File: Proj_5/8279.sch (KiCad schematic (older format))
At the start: 24 parts

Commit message: Labeled Data Bus and Address bus wires in CMOS
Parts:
- SW? (x22): symbol Proj_5_Custom_LED:Switch_SW_SPST -> Proj_5-rescue:Switch_SW_SPST-Proj_5_Custom_LED
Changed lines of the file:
@@
 	10050 6550 10050 5500
 $Comp
-L Proj_5_Custom_LED:Switch_SW_SPST SW?
+L Proj_5-rescue:Switch_SW_SPST-Proj_5_Custom_LED SW?
 U 1 1 5EA20375
 P 10250 3000
@@
 $EndComp
 $Comp
-L Proj_5_Custom_LED:Switch_SW_SPST SW?
+L Proj_5-rescue:Switch_SW_SPST-Proj_5_Custom_LED SW?
 U 1 1 5EA1576F
 P 10250 5000
@@
 $EndComp
 $Comp
-L Proj_5_Custom_LED:Switch_SW_SPST SW?
+L Proj_5-rescue:Switch_SW_SPST-Proj_5_Custom_LED SW?
 U 1 1 5EA154A2
 P 10250 4500
@@
 $EndComp
 $Comp
-L Proj_5_Custom_LED:Switch_SW_SPST SW?
+L Proj_5-rescue:Switch_SW_SPST-Proj_5_Custom_LED SW?
 U 1 1 5EA14DD7
 P 10250 4000
@@
 $EndComp
 $Comp
-L Proj_5_Custom_LED:Switch_SW_SPST SW?
+L Proj_5-rescue:Switch_SW_SPST-Proj_5_Custom_LED SW?
 U 1 1 5EA137C2
 P 10250 3500
@@
 	11600 3000 11450 3000
 $Comp
-L Proj_5_Custom_LED:Switch_SW_SPST SW?
+L Proj_5-rescue:Switch_SW_SPST-Proj_5_Custom_LED SW?
 U 1 1 5EA3DD7B
 P 11250 3000
@@
 $EndComp
 $Comp
-L Proj_5_Custom_LED:Switch_SW_SPST SW?
+L Proj_5-rescue:Switch_SW_SPST-Proj_5_Custom_LED SW?
 U 1 1 5EA3DD81
 P 11250 5000
@@
 $EndComp
 $Comp
-L Proj_5_Custom_LED:Switch_SW_SPST SW?
+L Proj_5-rescue:Switch_SW_SPST-Proj_5_Custom_LED SW?
 U 1 1 5EA3DD87
 P 11250 4500
@@
 $EndComp
 $Comp
-L Proj_5_Custom_LED:Switch_SW_SPST SW?
+L Proj_5-rescue:Switch_SW_SPST-Proj_5_Custom_LED SW?
 U 1 1 5EA3DD8D
 P 11250 4000
@@
 $EndComp
 $Comp
-L Proj_5_Custom_LED:Switch_SW_SPST SW?
+L Proj_5-rescue:Switch_SW_SPST-Proj_5_Custom_LED SW?
 U 1 1 5EA3DD93
 P 11250 3500
@@
 	12600 3500 12450 3500
 $Comp
-L Proj_5_Custom_LED:Switch_SW_SPST SW?
+L Proj_5-rescue:Switch_SW_SPST-Proj_5_Custom_LED SW?
 U 1 1 5EA78021
 P 12250 5000
@@
 $EndComp
 $Comp
-L Proj_5_Custom_LED:Switch_SW_SPST SW?
+L Proj_5-rescue:Switch_SW_SPST-Proj_5_Custom_LED SW?
 U 1 1 5EA78027
 P 12250 4500
@@
 $EndComp
 $Comp
-L Proj_5_Custom_LED:Switch_SW_SPST SW?
+L Proj_5-rescue:Switch_SW_SPST-Proj_5_Custom_LED SW?
 U 1 1 5EA7802D
 P 12250 4000
@@
 $EndComp
 $Comp
-L Proj_5_Custom_LED:Switch_SW_SPST SW?
+L Proj_5-rescue:Switch_SW_SPST-Proj_5_Custom_LED SW?
 U 1 1 5EA78033
 P 12250 3500
@@
 	13600 3500 13450 3500
 $Comp
-L Proj_5_Custom_LED:Switch_SW_SPST SW?
+L Proj_5-rescue:Switch_SW_SPST-Proj_5_Custom_LED SW?
 U 1 1 5EA82E83
 P 13250 5000
@@
 $EndComp
 $Comp
-L Proj_5_Custom_LED:Switch_SW_SPST SW?
+L Proj_5-rescue:Switch_SW_SPST-Proj_5_Custom_LED SW?
 U 1 1 5EA82E89
 P 13250 4500
@@
 $EndComp
 $Comp
-L Proj_5_Custom_LED:Switch_SW_SPST SW?
+L Proj_5-rescue:Switch_SW_SPST-Proj_5_Custom_LED SW?
 U 1 1 5EA82E8F
 P 13250 4000
@@
 $EndComp
 $Comp
-L Proj_5_Custom_LED:Switch_SW_SPST SW?
+L Proj_5-rescue:Switch_SW_SPST-Proj_5_Custom_LED SW?
 U 1 1 5EA82E95
 P 13250 3500
@@
 	14650 3500 14500 3500
 $Comp
-L Proj_5_Custom_LED:Switch_SW_SPST SW?
+L Proj_5-rescue:Switch_SW_SPST-Proj_5_Custom_LED SW?
 U 1 1 5EA89F25
 P 14300 5000
@@
 $EndComp
 $Comp
-L Proj_5_Custom_LED:Switch_SW_SPST SW?
+L Proj_5-rescue:Switch_SW_SPST-Proj_5_Custom_LED SW?
 U 1 1 5EA89F2B
 P 14300 4500
@@
 $EndComp
 $Comp
-L Proj_5_Custom_LED:Switch_SW_SPST SW?
+L Proj_5-rescue:Switch_SW_SPST-Proj_5_Custom_LED SW?
 U 1 1 5EA89F31
 P 14300 4000
@@
 $EndComp
 $Comp
-L Proj_5_Custom_LED:Switch_SW_SPST SW?
+L Proj_5-rescue:Switch_SW_SPST-Proj_5_Custom_LED SW?
 U 1 1 5EA89F37
 P 14300 3500

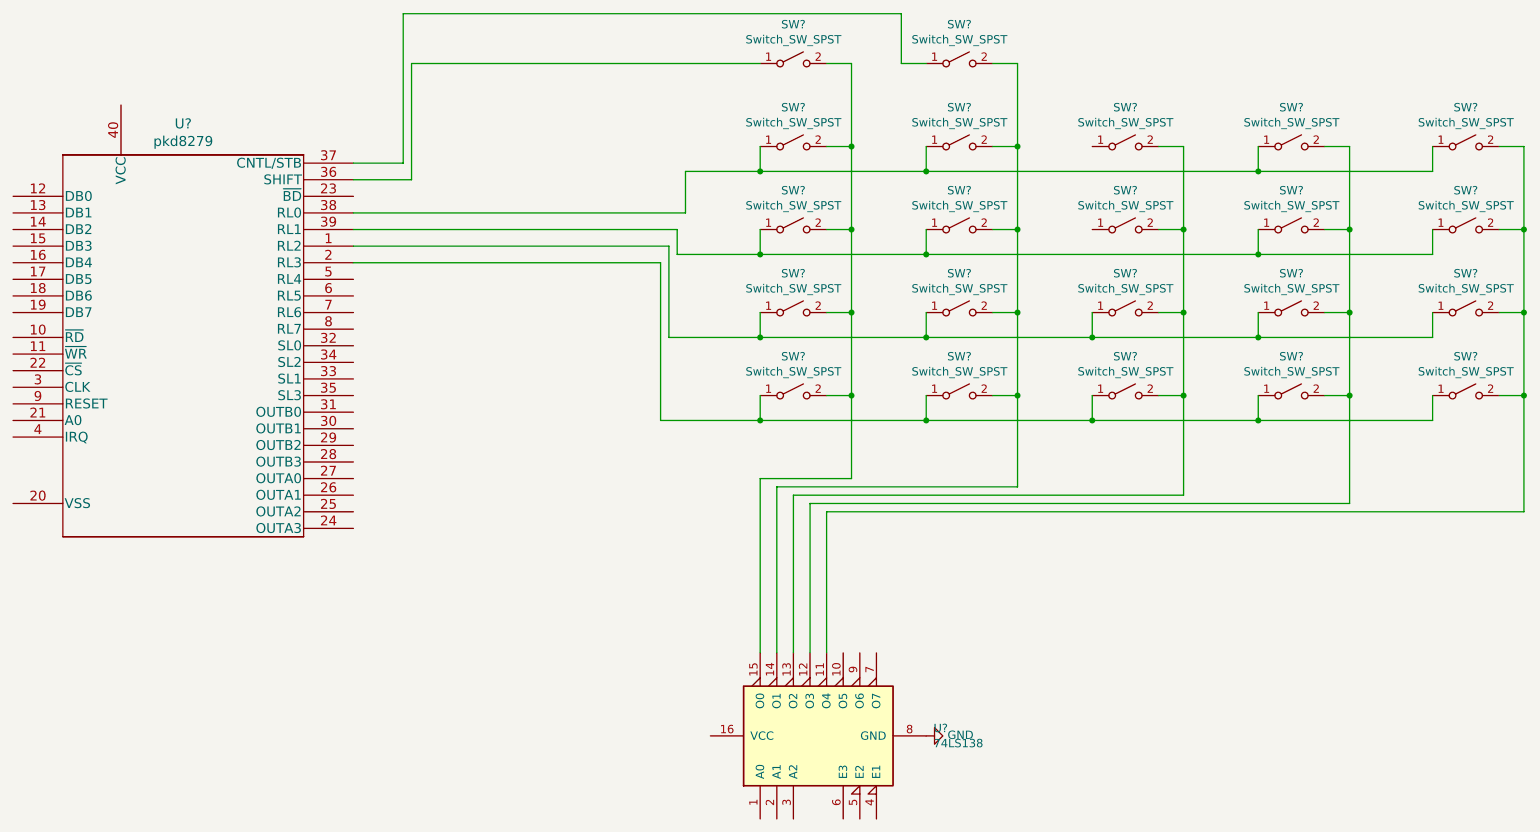
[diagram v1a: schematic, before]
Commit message: Added address decoding
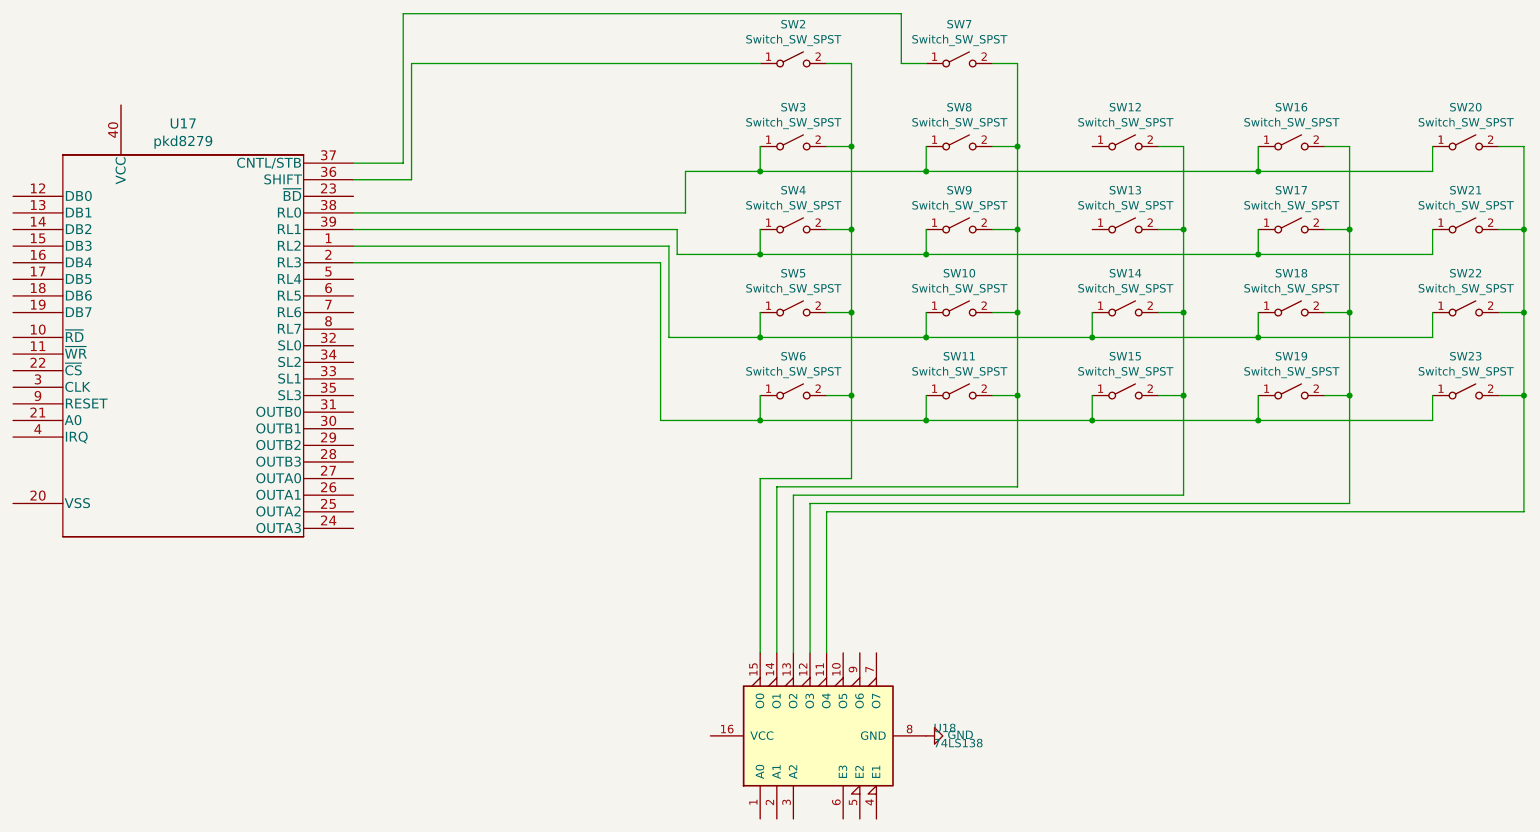
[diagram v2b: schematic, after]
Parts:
- gave numbers to parts that had none: 24
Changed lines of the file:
@@
 $EndDescr
 $Comp
-L pkd8279:pkd8279 U?
+L pkd8279:pkd8279 U17
 U 1 1 5EA03B7A
 P 5550 3750
-F 0 "U?" H 6575 4137 60  0000 C CNN
+F 0 "U17" H 6575 4137 60  0000 C CNN
 F 1 "pkd8279" H 6575 4031 60  0000 C CNN
 F 2 "pkd8279" H 6550 4140 60  0001 C CNN
@@
 $EndComp
 $Comp
-L 74xx:74LS138 U?
+L 74xx:74LS138 U18
 U 1 1 5EA0A47C
 P 10350 7050
-F 0 "U?" V 10396 6306 50  0000 R CNN
+F 0 "U18" V 10396 6306 50  0000 R CNN
 F 1 "74LS138" V 10305 6306 50  0000 R CNN
 F 2 "" H 10350 7050 50  0001 C CNN
@@
 $EndComp
 $Comp
-L power:GND #PWR?
+L power:GND #PWR0115
 U 1 1 5EA0B578
 P 11050 7050
-F 0 "#PWR?" H 11050 6800 50  0001 C CNN
+F 0 "#PWR0115" H 11050 6800 50  0001 C CNN
 F 1 "GND" V 11055 6922 50  0000 R CNN
 F 2 "" H 11050 7050 50  0001 C CNN
@@
 U 1 1 5EA20375
 P 10250 3000
-F 0 "SW?" H 10250 3235 50  0000 C CNN
+AR Path="/5EA20375" Ref="SW?"  Part="1"
+AR Path="/5EA993EC/5EA20375" Ref="SW2"  Part="1"
+F 0 "SW2" H 10250 3235 50  0000 C CNN
 F 1 "Switch_SW_SPST" H 10250 3144 50  0000 C CNN
 F 2 "" H 10250 3000 50  0001 C CNN
@@
 U 1 1 5EA1576F
 P 10250 5000
-F 0 "SW?" H 10250 5235 50  0000 C CNN
+AR Path="/5EA1576F" Ref="SW?"  Part="1"
+AR Path="/5EA993EC/5EA1576F" Ref="SW6"  Part="1"
+F 0 "SW6" H 10250 5235 50  0000 C CNN
 F 1 "Switch_SW_SPST" H 10250 5144 50  0000 C CNN
 F 2 "" H 10250 5000 50  0001 C CNN
@@
 U 1 1 5EA154A2
 P 10250 4500
-F 0 "SW?" H 10250 4735 50  0000 C CNN
+AR Path="/5EA154A2" Ref="SW?"  Part="1"
+AR Path="/5EA993EC/5EA154A2" Ref="SW5"  Part="1"
+F 0 "SW5" H 10250 4735 50  0000 C CNN
 F 1 "Switch_SW_SPST" H 10250 4644 50  0000 C CNN
 F 2 "" H 10250 4500 50  0001 C CNN
@@
 U 1 1 5EA14DD7
 P 10250 4000
-F 0 "SW?" H 10250 4235 50  0000 C CNN
+AR Path="/5EA14DD7" Ref="SW?"  Part="1"
+AR Path="/5EA993EC/5EA14DD7" Ref="SW4"  Part="1"
+F 0 "SW4" H 10250 4235 50  0000 C CNN
 F 1 "Switch_SW_SPST" H 10250 4144 50  0000 C CNN
 F 2 "" H 10250 4000 50  0001 C CNN
@@
 U 1 1 5EA137C2
 P 10250 3500
-F 0 "SW?" H 10250 3735 50  0000 C CNN
+AR Path="/5EA137C2" Ref="SW?"  Part="1"
+AR Path="/5EA993EC/5EA137C2" Ref="SW3"  Part="1"
+F 0 "SW3" H 10250 3735 50  0000 C CNN
 F 1 "Switch_SW_SPST" H 10250 3644 50  0000 C CNN
 F 2 "" H 10250 3500 50  0001 C CNN
@@
 U 1 1 5EA3DD7B
 P 11250 3000
-F 0 "SW?" H 11250 3235 50  0000 C CNN
+AR Path="/5EA3DD7B" Ref="SW?"  Part="1"
+AR Path="/5EA993EC/5EA3DD7B" Ref="SW7"  Part="1"
+F 0 "SW7" H 11250 3235 50  0000 C CNN
 F 1 "Switch_SW_SPST" H 11250 3144 50  0000 C CNN
 F 2 "" H 11250 3000 50  0001 C CNN
@@
 U 1 1 5EA3DD81
 P 11250 5000
-F 0 "SW?" H 11250 5235 50  0000 C CNN
+AR Path="/5EA3DD81" Ref="SW?"  Part="1"
+AR Path="/5EA993EC/5EA3DD81" Ref="SW11"  Part="1"
+F 0 "SW11" H 11250 5235 50  0000 C CNN
 F 1 "Switch_SW_SPST" H 11250 5144 50  0000 C CNN
 F 2 "" H 11250 5000 50  0001 C CNN
@@
 U 1 1 5EA3DD87
 P 11250 4500
-F 0 "SW?" H 11250 4735 50  0000 C CNN
+AR Path="/5EA3DD87" Ref="SW?"  Part="1"
+AR Path="/5EA993EC/5EA3DD87" Ref="SW10"  Part="1"
+F 0 "SW10" H 11250 4735 50  0000 C CNN
 F 1 "Switch_SW_SPST" H 11250 4644 50  0000 C CNN
 F 2 "" H 11250 4500 50  0001 C CNN
@@
 U 1 1 5EA3DD8D
 P 11250 4000
-F 0 "SW?" H 11250 4235 50  0000 C CNN
+AR Path="/5EA3DD8D" Ref="SW?"  Part="1"
+AR Path="/5EA993EC/5EA3DD8D" Ref="SW9"  Part="1"
+F 0 "SW9" H 11250 4235 50  0000 C CNN
 F 1 "Switch_SW_SPST" H 11250 4144 50  0000 C CNN
 F 2 "" H 11250 4000 50  0001 C CNN
@@
 U 1 1 5EA3DD93
 P 11250 3500
-F 0 "SW?" H 11250 3735 50  0000 C CNN
+AR Path="/5EA3DD93" Ref="SW?"  Part="1"
+AR Path="/5EA993EC/5EA3DD93" Ref="SW8"  Part="1"
+F 0 "SW8" H 11250 3735 50  0000 C CNN
 F 1 "Switch_SW_SPST" H 11250 3644 50  0000 C CNN
 F 2 "" H 11250 3500 50  0001 C CNN
@@
 U 1 1 5EA78021
 P 12250 5000
-F 0 "SW?" H 12250 5235 50  0000 C CNN
+AR Path="/5EA78021" Ref="SW?"  Part="1"
+AR Path="/5EA993EC/5EA78021" Ref="SW15"  Part="1"
+F 0 "SW15" H 12250 5235 50  0000 C CNN
 F 1 "Switch_SW_SPST" H 12250 5144 50  0000 C CNN
 F 2 "" H 12250 5000 50  0001 C CNN
@@
 U 1 1 5EA78027
 P 12250 4500
-F 0 "SW?" H 12250 4735 50  0000 C CNN
+AR Path="/5EA78027" Ref="SW?"  Part="1"
+AR Path="/5EA993EC/5EA78027" Ref="SW14"  Part="1"
+F 0 "SW14" H 12250 4735 50  0000 C CNN
 F 1 "Switch_SW_SPST" H 12250 4644 50  0000 C CNN
 F 2 "" H 12250 4500 50  0001 C CNN
@@
 U 1 1 5EA7802D
 P 12250 4000
-F 0 "SW?" H 12250 4235 50  0000 C CNN
+AR Path="/5EA7802D" Ref="SW?"  Part="1"
+AR Path="/5EA993EC/5EA7802D" Ref="SW13"  Part="1"
+F 0 "SW13" H 12250 4235 50  0000 C CNN
 F 1 "Switch_SW_SPST" H 12250 4144 50  0000 C CNN
 F 2 "" H 12250 4000 50  0001 C CNN
@@
 U 1 1 5EA78033
 P 12250 3500
-F 0 "SW?" H 12250 3735 50  0000 C CNN
+AR Path="/5EA78033" Ref="SW?"  Part="1"
+AR Path="/5EA993EC/5EA78033" Ref="SW12"  Part="1"
+F 0 "SW12" H 12250 3735 50  0000 C CNN
 F 1 "Switch_SW_SPST" H 12250 3644 50  0000 C CNN
 F 2 "" H 12250 3500 50  0001 C CNN
@@
 U 1 1 5EA82E83
 P 13250 5000
-F 0 "SW?" H 13250 5235 50  0000 C CNN
+AR Path="/5EA82E83" Ref="SW?"  Part="1"
+AR Path="/5EA993EC/5EA82E83" Ref="SW19"  Part="1"
+F 0 "SW19" H 13250 5235 50  0000 C CNN
 F 1 "Switch_SW_SPST" H 13250 5144 50  0000 C CNN
 F 2 "" H 13250 5000 50  0001 C CNN
@@
 U 1 1 5EA82E89
 P 13250 4500
-F 0 "SW?" H 13250 4735 50  0000 C CNN
+AR Path="/5EA82E89" Ref="SW?"  Part="1"
+AR Path="/5EA993EC/5EA82E89" Ref="SW18"  Part="1"
+F 0 "SW18" H 13250 4735 50  0000 C CNN
 F 1 "Switch_SW_SPST" H 13250 4644 50  0000 C CNN
 F 2 "" H 13250 4500 50  0001 C CNN
@@
 U 1 1 5EA82E8F
 P 13250 4000
-F 0 "SW?" H 13250 4235 50  0000 C CNN
+AR Path="/5EA82E8F" Ref="SW?"  Part="1"
+AR Path="/5EA993EC/5EA82E8F" Ref="SW17"  Part="1"
+F 0 "SW17" H 13250 4235 50  0000 C CNN
 F 1 "Switch_SW_SPST" H 13250 4144 50  0000 C CNN
 F 2 "" H 13250 4000 50  0001 C CNN
@@
 U 1 1 5EA82E95
 P 13250 3500
-F 0 "SW?" H 13250 3735 50  0000 C CNN
+AR Path="/5EA82E95" Ref="SW?"  Part="1"
+AR Path="/5EA993EC/5EA82E95" Ref="SW16"  Part="1"
+F 0 "SW16" H 13250 3735 50  0000 C CNN
 F 1 "Switch_SW_SPST" H 13250 3644 50  0000 C CNN
 F 2 "" H 13250 3500 50  0001 C CNN
@@
 U 1 1 5EA89F25
 P 14300 5000
-F 0 "SW?" H 14300 5235 50  0000 C CNN
+AR Path="/5EA89F25" Ref="SW?"  Part="1"
+AR Path="/5EA993EC/5EA89F25" Ref="SW23"  Part="1"
+F 0 "SW23" H 14300 5235 50  0000 C CNN
 F 1 "Switch_SW_SPST" H 14300 5144 50  0000 C CNN
 F 2 "" H 14300 5000 50  0001 C CNN
@@
 U 1 1 5EA89F2B
 P 14300 4500
-F 0 "SW?" H 14300 4735 50  0000 C CNN
+AR Path="/5EA89F2B" Ref="SW?"  Part="1"
+AR Path="/5EA993EC/5EA89F2B" Ref="SW22"  Part="1"
+F 0 "SW22" H 14300 4735 50  0000 C CNN
 F 1 "Switch_SW_SPST" H 14300 4644 50  0000 C CNN
 F 2 "" H 14300 4500 50  0001 C CNN
@@
 U 1 1 5EA89F31
 P 14300 4000
-F 0 "SW?" H 14300 4235 50  0000 C CNN
+AR Path="/5EA89F31" Ref="SW?"  Part="1"
+AR Path="/5EA993EC/5EA89F31" Ref="SW21"  Part="1"
+F 0 "SW21" H 14300 4235 50  0000 C CNN
 F 1 "Switch_SW_SPST" H 14300 4144 50  0000 C CNN
 F 2 "" H 14300 4000 50  0001 C CNN
@@
 U 1 1 5EA89F37
 P 14300 3500
-F 0 "SW?" H 14300 3735 50  0000 C CNN
+AR Path="/5EA89F37" Ref="SW?"  Part="1"
+AR Path="/5EA993EC/5EA89F37" Ref="SW20"  Part="1"
+F 0 "SW20" H 14300 3735 50  0000 C CNN
 F 1 "Switch_SW_SPST" H 14300 3644 50  0000 C CNN
 F 2 "" H 14300 3500 50  0001 C CNN

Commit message: Added Caps to Each Vcc per desc.
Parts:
- added C?: 0.1uF, symbol Device:C
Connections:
- net at SW16.1 (A), SW20.1 (A), SW3.1 (A)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: now also SW12.1 (A)
- net at SW17.1 (A), SW21.1 (A), SW4.1 (A)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: now also SW13.1 (A)
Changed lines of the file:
@@
 $Descr A2 23386 16535
 encoding utf-8
-Sheet 9 11
+Sheet 8 11
 Title ""
 Date ""
@@
 Connection ~ 11050 3650
 Wire Wire Line
-	11050 3650 13050 3650
+	11050 3650 12050 3650
 Wire Wire Line
 	11050 4000 11050 4150
 Connection ~ 11050 4150
 Wire Wire Line
-	11050 4150 13050 4150
-Wire Wire Line
 	11050 4500 11050 4650
 Connection ~ 11050 4650
@@
 	14100 5150 14100 5000
 Connection ~ 13050 5150
+Wire Wire Line
+	11050 4150 12050 4150
+Wire Wire Line
+	12050 4150 12050 4000
+Connection ~ 12050 4150
+Wire Wire Line
+	12050 4150 13050 4150
+Wire Wire Line
+	12050 3650 12050 3500
+Connection ~ 12050 3650
+Wire Wire Line
+	12050 3650 13050 3650
+$Comp
+L Device:C C?
+U 1 1 5EA655BD
+P 6550 3000
+AR Path="/5EA98353/5EA655BD" Ref="C?"  Part="1"
+AR Path="/5EA993EC/5EA655BD" Ref="C?"  Part="1"
+F 0 "C?" V 6298 3000 50  0000 C CNN
+F 1 "0.1uF" V 6389 3000 50  0000 C CNN
+F 2 "" H 6588 2850 50  0001 C CNN
+F 3 "~" H 6550 3000 50  0001 C CNN
+	1    6550 3000
+	0    1    1    0
+$EndComp
 $EndSCHEMATC
